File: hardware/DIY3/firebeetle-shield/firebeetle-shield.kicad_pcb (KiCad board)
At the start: 2 copper layers, 30 x 72 mm, 6 parts, among them J1 Conn_01x14_Female, J2 Conn_01x06_Female (DS3231), J3 Conn_01x06_Female (microSD), J4 Conn_01x04_Male (JST to MS580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, J5 Conn_01x18_Female

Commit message: Finish shield design
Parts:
- added JP1: SolderJumper_2_Bridged, Jumper:SolderJumper-2_P1.3mm_Bridged_RoundedPad1.0x1.5mm, B.Cu at (121.3, 156.9)
- added JP2: SolderJumper_2_Bridged, Jumper:SolderJumper-2_P1.3mm_Bridged_RoundedPad1.0x1.5mm, B.Cu at (118.8, 156.9)
- added REF**: PinSocket_1x08_P2.54mm_Vertical, Connector_PinSocket_2.54mm:PinSocket_1x08_P2.54mm_Vertical, F.Cu at (106.1, 150.8)
- J3: renamed from J4; value Conn_01x04_Male (JST to MS5803) -> Conn_01x04_Male (MS5803)
- JP3: renamed from JP1; moved to B.Cu
- turned JP3 to -90 degrees
- renumbered J3 to J4
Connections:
- J1 pad 1: D10 -> VCC
- J1 pad 10: SDA -> A0
- J1 pad 11: SCL -> D13
- J1 pad 12: GND -> D12
- J1 pad 13: 3V3 -> D11
- J1 pad 14: VCC -> D10
- J1 pad 2: D11 -> 3V3
- J1 pad 3: D12 -> GND
- J1 pad 4: D13 -> SCL
- J1 pad 5: A0 -> SDA
- J1 pad 6: A1 -> A4
- J1 pad 7: A2 -> A3
- J1 pad 8: A3 -> A2
- J1 pad 9: A4 -> A1
- J2 pad 1: 32K -> Net-(J2-Pad1)
- J2 pad 2: SQW -> Net-(J2-Pad2)
- J5 pad 1: RX -> RST
- J5 pad 10: SCL -> SDA
- J5 pad 11: MISO -> CS
- J5 pad 12: MOSI -> D7
- J5 pad 13: SCK -> D6
- J5 pad 14: EN -> D5
- J5 pad 15: GND -> D3
- J5 pad 16: NONE -> D2
- J5 pad 17: 3V3 -> TX
- J5 pad 18: RST -> RX
- J5 pad 2: TX -> 3V3
- J5 pad 3: D2 -> NONE
- J5 pad 4: D3 -> GND
- J5 pad 5: D5 -> EN
- J5 pad 6: D6 -> SCK
- J5 pad 7: D7 -> MOSI
- J5 pad 8: D9 -> MISO
- J5 pad 9: SDA -> SCL
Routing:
- net CS: track 0.00 -> 50.5 mm
- net SCL: track 29.7 -> 61.4 mm
- net SDA: track 33.6 -> 62.3 mm
- net D2: track 0.00 -> 26.9 mm
- net MISO: track 27.9 -> 33.5 mm, vias 1 -> 0
- net 32K: track 0.00 -> 5.45 mm
- net SCK: track 35.5 -> 30.8 mm, vias 1 -> 0
- net Net-(J2-Pad2): track 0.00 -> 3.41 mm
- net Net-(J2-Pad1): track 0.00 -> 3.41 mm
- net MOSI: track 35.5 -> 37.9 mm, vias 1 -> 0
- net GND: vias 0 -> 3
- added copper zone on B.Cu, net GND
- added copper zone on F.Cu, net GND
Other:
- board size 30 x 72 mm -> 34 x 72 mm
- board text added: "32K"
- board text added: "32K ↓"
- board text added: "3V3"
- board text added: "3V3 to RTC"
- board text added: "A0"
- board text added: "A1"
- board text added: "A3"
- board text added: "A4"
- board text added: "CS"
- board text added: "D10"
- board text added: "D11"
- board text added: "D12"
- board text added: "D13"
- board text added: "D2"
- board text added: "D3"
- board text added: "D5"
- board text added: "D6"
- board text added: "D7"
- board text added: "D9"
- board text added: "DIY3: FireBeetle Shield V1"
- board text added: "DS3231(SN/M)"
- board text added: "EN"
- board text added: "GND"
- board text added: "MI"
- board text added: "MISO"
- board text added: "MO"
- board text added: "MOSI"
- board text added: "MS5803"
- board text added: "RST"
- board text added: "RX"
- board text added: "SCK"
- board text added: "SCL"
- board text added: "SDA"
- board text added: "SQW"
- board text added: "SQW to D2"
- board text added: "TX"
- board text added: "UWindsor Coastal Group"
- board text added: "VCC"
- board text added: "microSD"

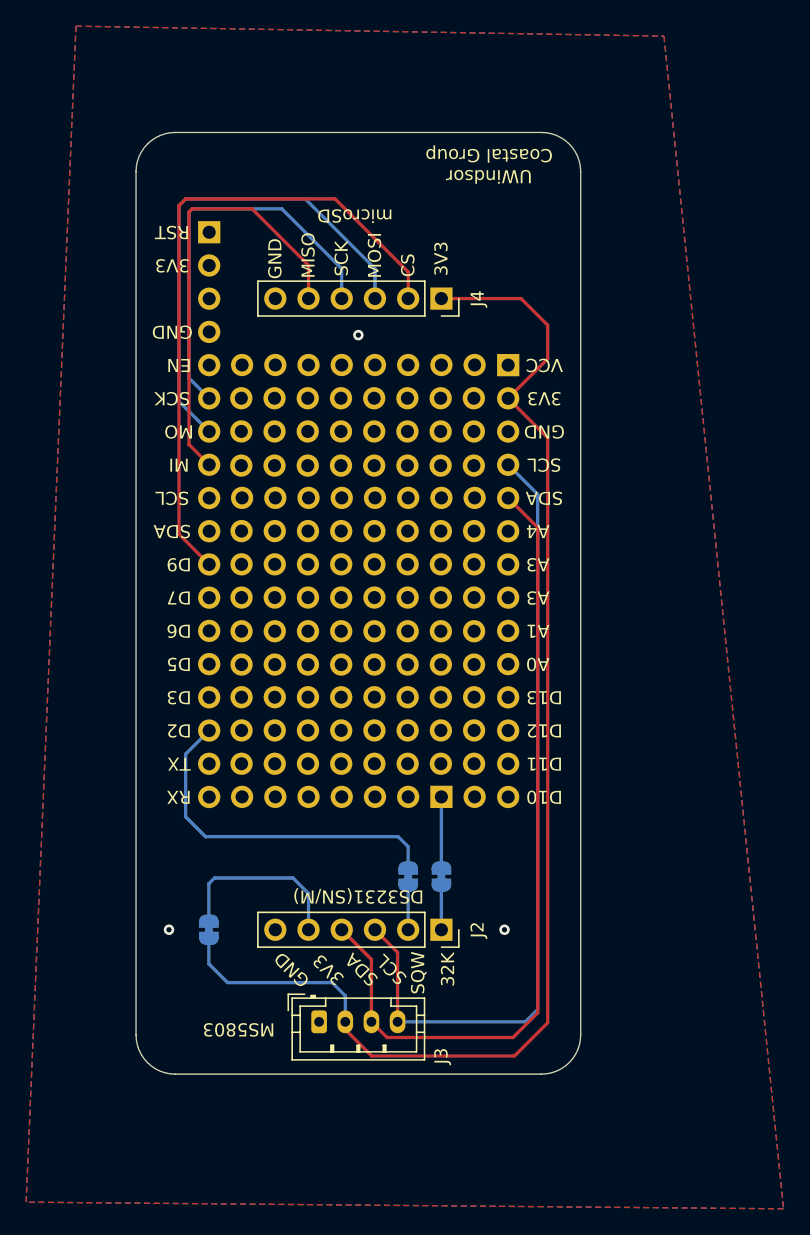
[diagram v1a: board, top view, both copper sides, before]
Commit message: Rotate board PCB and regenerate gerbers+drill files (not manufactured version)
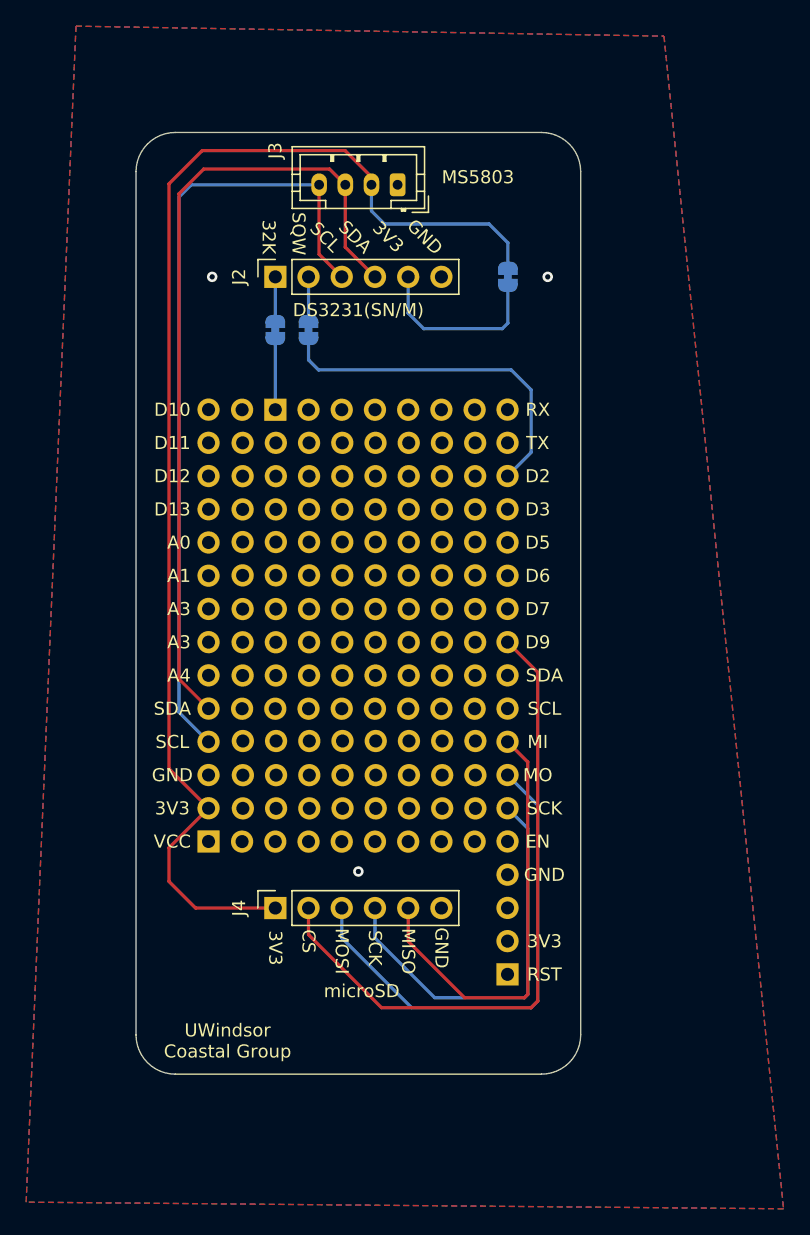
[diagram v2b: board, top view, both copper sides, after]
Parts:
- moved J3 64.3 mm to (118.0, 104.0), turned to 180 degrees
- moved J5 61.2 mm to (126.4, 164.4), turned to 0 degrees
- moved JP3 54.9 mm to (126.4, 111.0), turned to 90 degrees
- moved J2 51.5 mm to (108.7, 111.0), turned to 90 degrees
- moved J4 48.3 mm to (108.7, 159.3), turned to 90 degrees
- moved JP1 43.7 mm to (108.7, 115.1), turned to -90 degrees
- moved J1 43.0 mm to (103.5, 154.2), turned to 0 degrees
- moved JP2 42.5 mm to (111.2, 115.1), turned to -90 degrees
- moved REF** 34.5 mm to (123.9, 121.2), turned to -90 degrees

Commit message: Add change notes for next iteration to design
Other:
- board text added: "Notes for next iteration: - put shield header pin outline on front silkscreen - maybe change JST pin spacing to 2.54 mm instead of 2 mm - change {dblquote}UWindsor Coastal Group{dblquote} to {dblquote}Windsor Coastal Group{dblquote} and increase font size - include group logo"
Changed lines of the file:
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@@
     (effects (font (size 1 1) (thickness 0.15)))
+  )
+  (gr_text "Notes for next iteration:\n- put shield header pin outline on front silkscreen\n- maybe change JST pin spacing to 2.54 mm instead of 2 mm\n- change {dblquote}UWindsor Coastal Group{dblquote} to {dblquote}Windsor Coastal Group{dblquote} and increase font size\n- include group logo" (at 143 97) (layer "Cmts.User")
+    (effects (font (size 1 1) (thickness 0.15)) (justify left))
   )
   (segment (start 101.284 141.789) (end 103.545 144.05) (width 0.25) (layer "F.Cu") (net 1))
